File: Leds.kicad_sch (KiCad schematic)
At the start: 51 parts

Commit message: Updated power section. Updated all possible footprints to be "hand solder" version. Updated Symbol lib.
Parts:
- C1, C10, C11, C12, C13, C14, C15, C16, C17, C18, C19, C2, C20, C21, C22, C23, C24, C25, C26, C3, C4, C5, C6, C7, C8, C9: footprint Capacitor_SMD:C_0603_1608Metric -> Capacitor_SMD:C_0603_1608Metric_Pad1.08x0.95mm_HandSolder
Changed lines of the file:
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@@
       (effects (font (size 1.27 1.27)) (justify left))
     )
-    (property "Footprint" "Capacitor_SMD:C_0603_1608Metric" (id 2) (at 25.0952 113.03 0)
+    (property "Footprint" "Capacitor_SMD:C_0603_1608Metric_Pad1.08x0.95mm_HandSolder" (id 2) (at 25.0952 113.03 0)
       (effects (font (size 1.27 1.27)) hide)
     )
@@
       (effects (font (size 1.27 1.27)) (justify left))
     )
-    (property "Footprint" "Capacitor_SMD:C_0603_1608Metric" (id 2) (at 107.6452 93.98 0)
+    (property "Footprint" "Capacitor_SMD:C_0603_1608Metric_Pad1.08x0.95mm_HandSolder" (id 2) (at 107.6452 93.98 0)
       (effects (font (size 1.27 1.27)) hide)
     )
@@
       (effects (font (size 1.27 1.27)) (justify left))
     )
-    (property "Footprint" "Capacitor_SMD:C_0603_1608Metric" (id 2) (at 96.2152 93.98 0)
+    (property "Footprint" "Capacitor_SMD:C_0603_1608Metric_Pad1.08x0.95mm_HandSolder" (id 2) (at 96.2152 93.98 0)
       (effects (font (size 1.27 1.27)) hide)
     )
@@
       (effects (font (size 1.27 1.27)) (justify left))
     )
-    (property "Footprint" "Capacitor_SMD:C_0603_1608Metric" (id 2) (at 83.5152 93.98 0)
+    (property "Footprint" "Capacitor_SMD:C_0603_1608Metric_Pad1.08x0.95mm_HandSolder" (id 2) (at 83.5152 93.98 0)
       (effects (font (size 1.27 1.27)) hide)
     )
@@
       (effects (font (size 1.27 1.27)) (justify left))
     )
-    (property "Footprint" "Capacitor_SMD:C_0603_1608Metric" (id 2) (at 72.0852 93.98 0)
+    (property "Footprint" "Capacitor_SMD:C_0603_1608Metric_Pad1.08x0.95mm_HandSolder" (id 2) (at 72.0852 93.98 0)
       (effects (font (size 1.27 1.27)) hide)
     )
@@
       (effects (font (size 1.27 1.27)) (justify left))
     )
-    (property "Footprint" "Capacitor_SMD:C_0603_1608Metric" (id 2) (at 60.6552 93.98 0)
+    (property "Footprint" "Capacitor_SMD:C_0603_1608Metric_Pad1.08x0.95mm_HandSolder" (id 2) (at 60.6552 93.98 0)
       (effects (font (size 1.27 1.27)) hide)
     )
@@
       (effects (font (size 1.27 1.27)) (justify left))
     )
-    (property "Footprint" "Capacitor_SMD:C_0603_1608Metric" (id 2) (at 49.2252 93.98 0)
+    (property "Footprint" "Capacitor_SMD:C_0603_1608Metric_Pad1.08x0.95mm_HandSolder" (id 2) (at 49.2252 93.98 0)
       (effects (font (size 1.27 1.27)) hide)
     )
@@
       (effects (font (size 1.27 1.27)) (justify left))
     )
-    (property "Footprint" "Capacitor_SMD:C_0603_1608Metric" (id 2) (at 36.5252 93.98 0)
+    (property "Footprint" "Capacitor_SMD:C_0603_1608Metric_Pad1.08x0.95mm_HandSolder" (id 2) (at 36.5252 93.98 0)
       (effects (font (size 1.27 1.27)) hide)
     )
@@
       (effects (font (size 1.27 1.27)) (justify left))
     )
-    (property "Footprint" "Capacitor_SMD:C_0603_1608Metric" (id 2) (at 25.0952 93.98 0)
+    (property "Footprint" "Capacitor_SMD:C_0603_1608Metric_Pad1.08x0.95mm_HandSolder" (id 2) (at 25.0952 93.98 0)
       (effects (font (size 1.27 1.27)) hide)
     )
@@
       (effects (font (size 1.27 1.27)) (justify left))
     )
-    (property "Footprint" "Capacitor_SMD:C_0603_1608Metric" (id 2) (at 107.6452 74.93 0)
+    (property "Footprint" "Capacitor_SMD:C_0603_1608Metric_Pad1.08x0.95mm_HandSolder" (id 2) (at 107.6452 74.93 0)
       (effects (font (size 1.27 1.27)) hide)
     )
@@
       (effects (font (size 1.27 1.27)) (justify left))
     )
-    (property "Footprint" "Capacitor_SMD:C_0603_1608Metric" (id 2) (at 96.2152 74.93 0)
+    (property "Footprint" "Capacitor_SMD:C_0603_1608Metric_Pad1.08x0.95mm_HandSolder" (id 2) (at 96.2152 74.93 0)
       (effects (font (size 1.27 1.27)) hide)
     )
@@
       (effects (font (size 1.27 1.27)) (justify left))
     )
-    (property "Footprint" "Capacitor_SMD:C_0603_1608Metric" (id 2) (at 83.5152 74.93 0)
+    (property "Footprint" "Capacitor_SMD:C_0603_1608Metric_Pad1.08x0.95mm_HandSolder" (id 2) (at 83.5152 74.93 0)
       (effects (font (size 1.27 1.27)) hide)
     )
@@
       (effects (font (size 1.27 1.27)) (justify left))
     )
-    (property "Footprint" "Capacitor_SMD:C_0603_1608Metric" (id 2) (at 72.0852 74.93 0)
+    (property "Footprint" "Capacitor_SMD:C_0603_1608Metric_Pad1.08x0.95mm_HandSolder" (id 2) (at 72.0852 74.93 0)
       (effects (font (size 1.27 1.27)) hide)
     )
@@
       (effects (font (size 1.27 1.27)) (justify left))
     )
-    (property "Footprint" "Capacitor_SMD:C_0603_1608Metric" (id 2) (at 60.6552 74.93 0)
+    (property "Footprint" "Capacitor_SMD:C_0603_1608Metric_Pad1.08x0.95mm_HandSolder" (id 2) (at 60.6552 74.93 0)
       (effects (font (size 1.27 1.27)) hide)
     )
@@
       (effects (font (size 1.27 1.27)) (justify left))
     )
-    (property "Footprint" "Capacitor_SMD:C_0603_1608Metric" (id 2) (at 49.2252 74.93 0)
+    (property "Footprint" "Capacitor_SMD:C_0603_1608Metric_Pad1.08x0.95mm_HandSolder" (id 2) (at 49.2252 74.93 0)
       (effects (font (size 1.27 1.27)) hide)
     )
@@
       (effects (font (size 1.27 1.27)) (justify left))
     )
-    (property "Footprint" "Capacitor_SMD:C_0603_1608Metric" (id 2) (at 36.5252 74.93 0)
+    (property "Footprint" "Capacitor_SMD:C_0603_1608Metric_Pad1.08x0.95mm_HandSolder" (id 2) (at 36.5252 74.93 0)
       (effects (font (size 1.27 1.27)) hide)
     )
@@
       (effects (font (size 1.27 1.27)) (justify left))
     )
-    (property "Footprint" "Capacitor_SMD:C_0603_1608Metric" (id 2) (at 25.0952 74.93 0)
+    (property "Footprint" "Capacitor_SMD:C_0603_1608Metric_Pad1.08x0.95mm_HandSolder" (id 2) (at 25.0952 74.93 0)
       (effects (font (size 1.27 1.27)) hide)
     )
@@
       (effects (font (size 1.27 1.27)) (justify left))
     )
-    (property "Footprint" "Capacitor_SMD:C_0603_1608Metric" (id 2) (at 37.7952 113.03 0)
+    (property "Footprint" "Capacitor_SMD:C_0603_1608Metric_Pad1.08x0.95mm_HandSolder" (id 2) (at 37.7952 113.03 0)
       (effects (font (size 1.27 1.27)) hide)
     )
@@
       (effects (font (size 1.27 1.27)) (justify left))
     )
-    (property "Footprint" "Capacitor_SMD:C_0603_1608Metric" (id 2) (at 25.0952 40.64 0)
+    (property "Footprint" "Capacitor_SMD:C_0603_1608Metric_Pad1.08x0.95mm_HandSolder" (id 2) (at 25.0952 40.64 0)
       (effects (font (size 1.27 1.27)) hide)
     )
@@
       (effects (font (size 1.27 1.27)) (justify left))
     )
-    (property "Footprint" "Capacitor_SMD:C_0603_1608Metric" (id 2) (at 36.5252 40.64 0)
+    (property "Footprint" "Capacitor_SMD:C_0603_1608Metric_Pad1.08x0.95mm_HandSolder" (id 2) (at 36.5252 40.64 0)
       (effects (font (size 1.27 1.27)) hide)
     )
@@
       (effects (font (size 1.27 1.27)) (justify left))
     )
-    (property "Footprint" "Capacitor_SMD:C_0603_1608Metric" (id 2) (at 49.2252 40.64 0)
+    (property "Footprint" "Capacitor_SMD:C_0603_1608Metric_Pad1.08x0.95mm_HandSolder" (id 2) (at 49.2252 40.64 0)
       (effects (font (size 1.27 1.27)) hide)
     )
@@
       (effects (font (size 1.27 1.27)) (justify left))
     )
-    (property "Footprint" "Capacitor_SMD:C_0603_1608Metric" (id 2) (at 60.6552 40.64 0)
+    (property "Footprint" "Capacitor_SMD:C_0603_1608Metric_Pad1.08x0.95mm_HandSolder" (id 2) (at 60.6552 40.64 0)
       (effects (font (size 1.27 1.27)) hide)
     )
@@
       (effects (font (size 1.27 1.27)) (justify left))
     )
-    (property "Footprint" "Capacitor_SMD:C_0603_1608Metric" (id 2) (at 72.0852 40.64 0)
+    (property "Footprint" "Capacitor_SMD:C_0603_1608Metric_Pad1.08x0.95mm_HandSolder" (id 2) (at 72.0852 40.64 0)
       (effects (font (size 1.27 1.27)) hide)
     )
@@
       (effects (font (size 1.27 1.27)) (justify left))
     )
-    (property "Footprint" "Capacitor_SMD:C_0603_1608Metric" (id 2) (at 83.5152 40.64 0)
+    (property "Footprint" "Capacitor_SMD:C_0603_1608Metric_Pad1.08x0.95mm_HandSolder" (id 2) (at 83.5152 40.64 0)
       (effects (font (size 1.27 1.27)) hide)
     )
@@
       (effects (font (size 1.27 1.27)) (justify left))
     )
-    (property "Footprint" "Capacitor_SMD:C_0603_1608Metric" (id 2) (at 96.2152 40.64 0)
+    (property "Footprint" "Capacitor_SMD:C_0603_1608Metric_Pad1.08x0.95mm_HandSolder" (id 2) (at 96.2152 40.64 0)
       (effects (font (size 1.27 1.27)) hide)
     )
@@
       (effects (font (size 1.27 1.27)) (justify left))
     )
-    (property "Footprint" "Capacitor_SMD:C_0603_1608Metric" (id 2) (at 107.6452 40.64 0)
-      (effects (font (size 1.27 1.27)) hide)
-    )
+    (property "Footprint" "Capacitor_SMD:C_0603_1608Metric_Pad1.08x0.95mm_HandSolder" (id 2) (at 107.6452 40.64 0)
+      (effects (font (size 1.27 1.27)) hide)
+    )

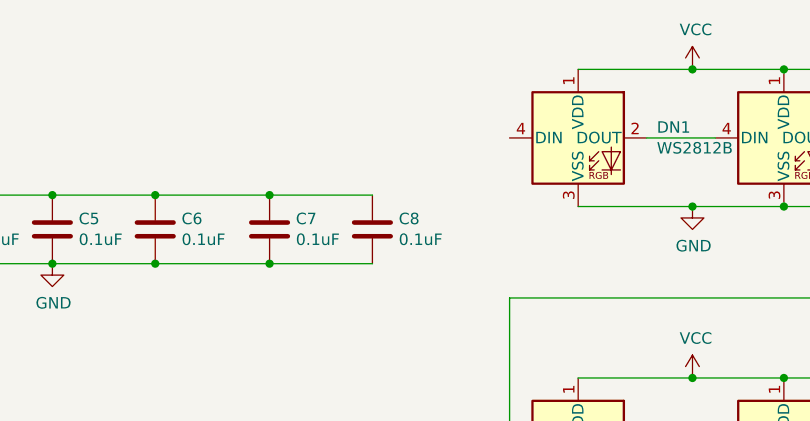
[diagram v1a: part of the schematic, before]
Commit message: ... Forgot to connect the data line to esp32... It's done now.
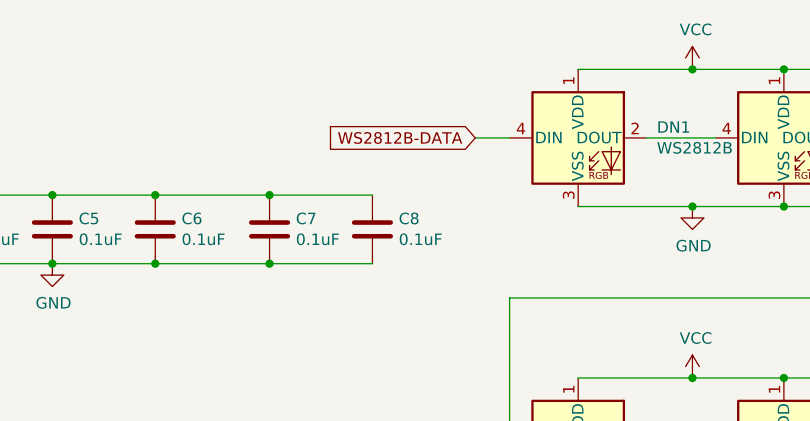
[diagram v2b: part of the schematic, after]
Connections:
- net WS2812B-DATA: now reaches DN1.4 (DIN)
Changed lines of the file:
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@@
   (junction (at 243.84 68.58) (diameter 0) (color 0 0 0 0)
   )
+  (junction (at 142.24 104.14) (diameter 0) (color 0 0 0 0)
+  )
   (junction (at 175.26 119.38) (diameter 0) (color 0 0 0 0)
   )
@@
   )
   (junction (at 48.26 74.93) (diameter 0) (color 0 0 0 0)
-  )
-  (junction (at 142.24 104.14) (diameter 0) (color 0 0 0 0)
   )
   (junction (at 82.55 93.98) (diameter 0) (color 0 0 0 0)
@@
     (stroke (width 0) (type default) (color 0 0 0 0))
   )
+  (wire (pts (xy 142.24 104.14) (xy 152.4 104.14))
+    (stroke (width 0) (type default) (color 0 0 0 0))
+  )
   (wire (pts (xy 82.55 33.02) (xy 95.25 33.02))
     (stroke (width 0) (type default) (color 0 0 0 0))
@@
     (stroke (width 0) (type default) (color 0 0 0 0))
   )
+  (wire (pts (xy 118.11 26.67) (xy 121.92 26.67))
+    (stroke (width 0) (type default) (color 0 0 0 0))
+  )
   (wire (pts (xy 142.24 119.38) (xy 152.4 119.38))
     (stroke (width 0) (type default) (color 0 0 0 0))
@@
     (stroke (width 0) (type default) (color 0 0 0 0))
   )
-  (wire (pts (xy 142.24 104.14) (xy 152.4 104.14))
-    (stroke (width 0) (type default) (color 0 0 0 0))
-  )
   (wire (pts (xy 243.84 19.05) (xy 220.98 19.05))
     (stroke (width 0) (type default) (color 0 0 0 0))
@@
     (stroke (width 0) (type default) (color 0 0 0 0))
   )
+  (global_label "WS2812B-DATA" (shape input) (at 118.11 26.67 180) (fields_autoplaced)
+    (effects (font (size 1.27 1.27)) (justify right))
+    (property "Intersheet References" "${INTERSHEET_REFS}" (id 0) (at 101.0296 26.5906 0)
+      (effects (font (size 1.27 1.27)) (justify right) hide)
+    )
+  )
   (symbol (lib_id "power:GND") (at 24.13 115.57 0) (unit 1)
